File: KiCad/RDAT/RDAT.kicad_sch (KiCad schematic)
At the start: 17 parts

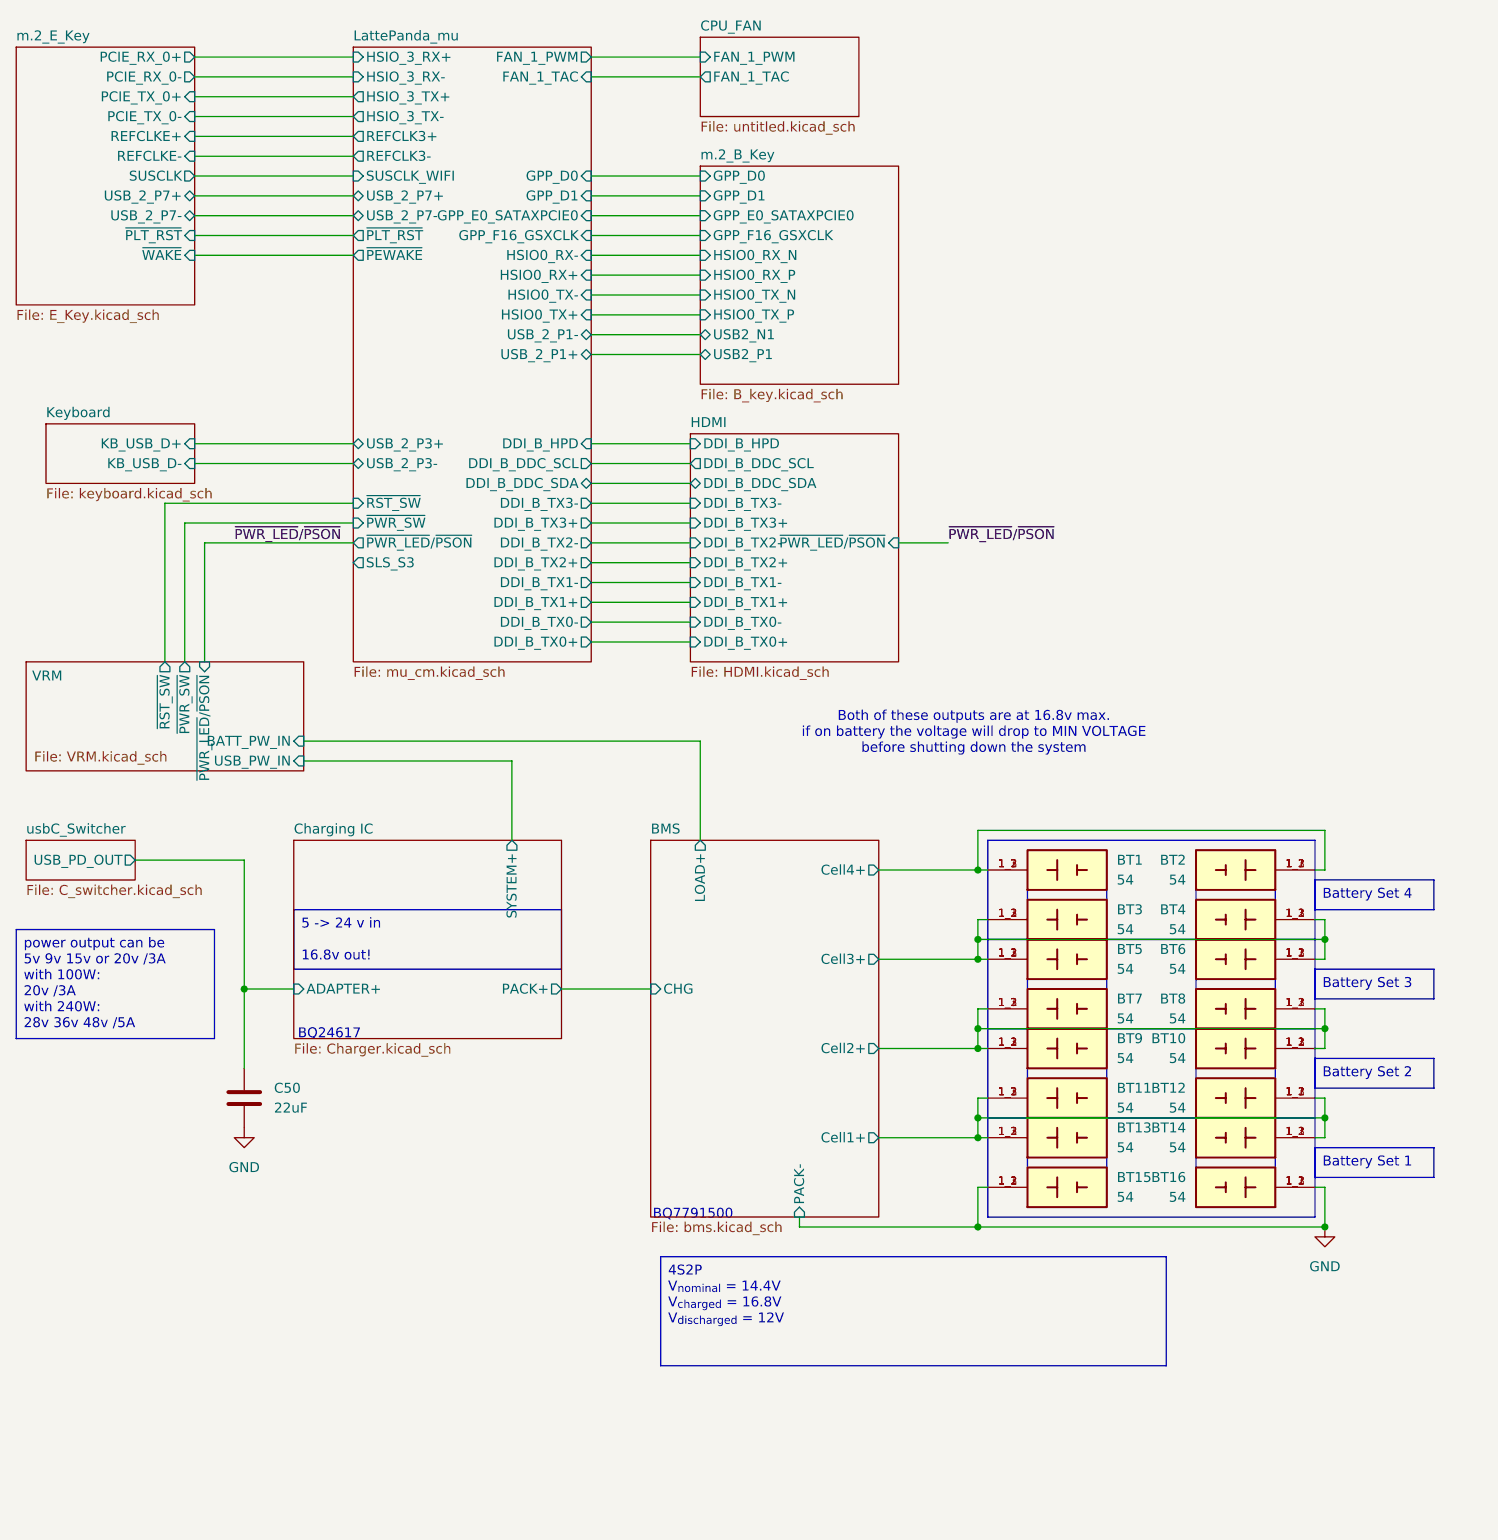
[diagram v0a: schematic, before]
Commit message: Started process of BMS review
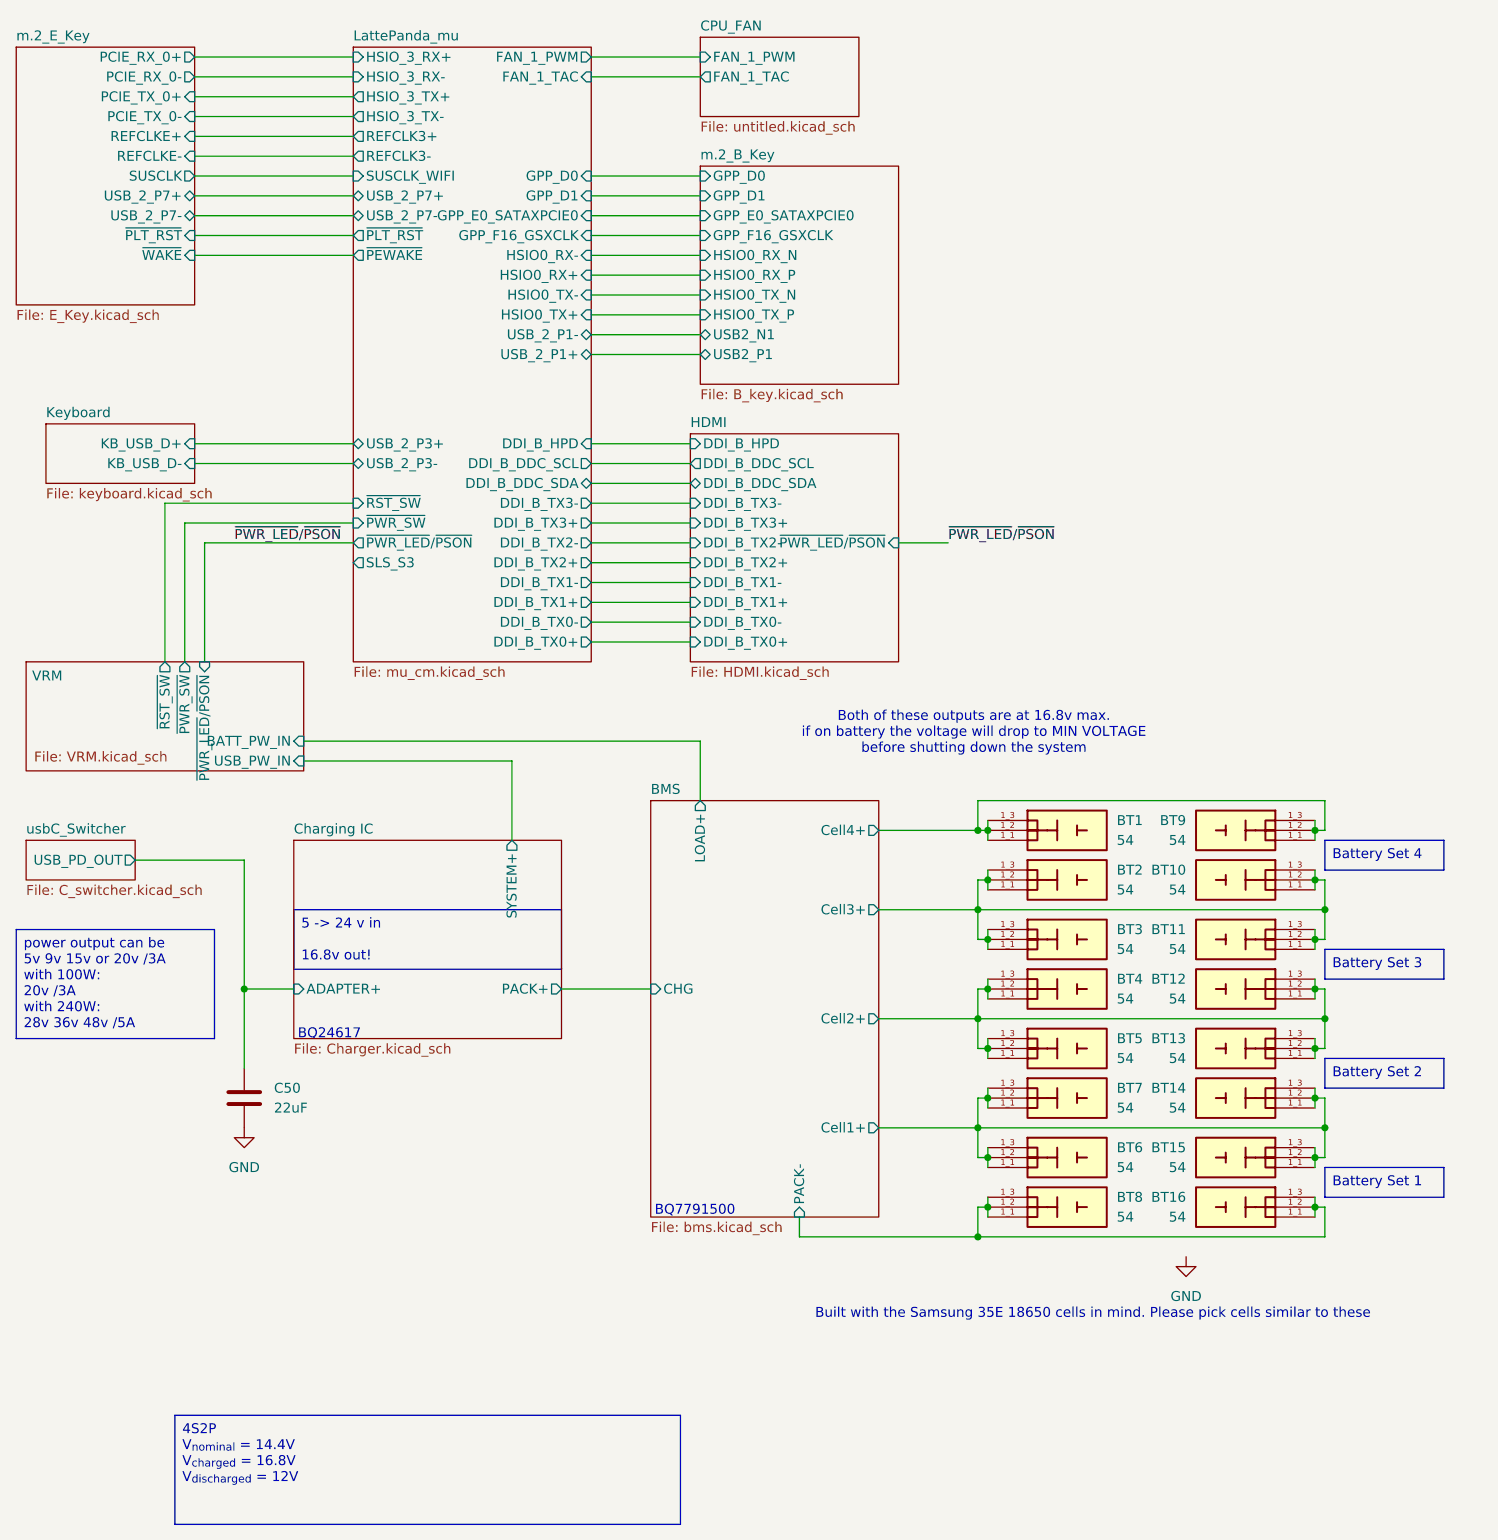
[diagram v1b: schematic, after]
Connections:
- net BMS/Cell1+: now also BT15.1_1, BT15.1_2, BT15.1_3, BT6.1_1, BT6.1_2, BT6.1_3, BT7.1_1, BT7.1_2, BT7.1_3; no longer BT11.1_1, BT11.1_2, BT11.1_3, BT12.1_1, BT12.1_2, BT12.1_3, BT13.1_1, BT13.1_2, BT13.1_3
- net BMS/Cell2+: now also BT12.1_1, BT12.1_2, BT12.1_3, BT13.1_1, BT13.1_2, BT13.1_3, BT4.1_1, BT4.1_2, BT4.1_3, BT5.1_1, BT5.1_2, BT5.1_3; no longer BT10.1_1, BT10.1_2, BT10.1_3, BT7.1_1, BT7.1_2, BT7.1_3, BT8.1_1, BT8.1_2, BT8.1_3, BT9.1_1, BT9.1_2, BT9.1_3
- net BMS/Cell3+: now also BT10.1_1, BT10.1_2, BT10.1_3, BT11.1_1, BT11.1_2, BT11.1_3, BT2.1_1, BT2.1_2, BT2.1_3; no longer BT4.1_1, BT4.1_2, BT4.1_3, BT5.1_1, BT5.1_2, BT5.1_3, BT6.1_1, BT6.1_2, BT6.1_3
- net BMS/Cell4+: now also BT9.1_1, BT9.1_2, BT9.1_3; no longer BT2.1_1, BT2.1_2, BT2.1_3
- net GND: no longer BT15.1_1, BT15.1_2, BT15.1_3, BT16.1_1, BT16.1_2, BT16.1_3
- new net BMS/PACK-: BT16.1_1, BT16.1_2, BT16.1_3, BT8.1_1, BT8.1_2, BT8.1_3
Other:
- note added: "Built with the Samsung 35E 18650 cells in mind. Please pick cells similar to these"

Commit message: 2x checked all schematics
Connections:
- net BMS/PACK- renamed Earth
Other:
- added sheet USBA_2.0 (usb.kicad_sch)
- sheet BMS ports: added SYS_BAT+, SYS_BAT-; removed CHG, LOAD+, PACK-
- sheet LattePanda_mu ports: added USB_2_P2+, USB_2_P2-, USB_2_P4+, USB_2_P4-; removed none

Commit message: Pre-Annotate FULL, add usb
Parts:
- BT1, BT10, BT11, BT12, BT13, BT14, BT15, BT16, BT2, BT3, BT4, BT5, BT6, BT7, BT8, BT9: JLCPCB_LINK (none) -> https://jlcpcb.com/partdetail/Keystone-54/C2685232
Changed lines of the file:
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@@
 			)
 		)
-		(property "Datasheet" ""
+		(property "Datasheet" "https://www.lcsc.com/datasheet/lcsc_datasheet_2103051836_Keystone-54_C2685232.pdf"
 			(at 173.99 116.84 0)
 			(effects
@@
 			)
 		)
+		(property "JLCPCB_LINK" "https://jlcpcb.com/partdetail/Keystone-54/C2685232"
+			(at 173.99 116.84 0)
+			(effects
+				(font
+					(size 1.27 1.27)
+				)
+				(hide yes)
+			)
+		)
 		(pin "1_3"
 		)
@@
 			)
 		)
-		(property "Datasheet" ""
+		(property "Datasheet" "https://www.lcsc.com/datasheet/lcsc_datasheet_2103051836_Keystone-54_C2685232.pdf"
 			(at 173.99 144.78 0)
 			(effects
@@
 			)
 		)
+		(property "JLCPCB_LINK" "https://jlcpcb.com/partdetail/Keystone-54/C2685232"
+			(at 173.99 144.78 0)
+			(effects
+				(font
+					(size 1.27 1.27)
+				)
+				(hide yes)
+			)
+		)
 		(pin "1_3"
 		)
@@
 			)
 		)
+		(property "JLCPCB_LINK" ""
+			(at 46.99 151.13 0)
+			(effects
+				(font
+					(size 1.27 1.27)
+				)
+			)
+		)
 		(pin "1"
 		)
@@
 			)
 		)
-		(property "Datasheet" ""
+		(property "Datasheet" "https://www.lcsc.com/datasheet/lcsc_datasheet_2103051836_Keystone-54_C2685232.pdf"
 			(at 173.99 151.13 0)
 			(effects
@@
 			)
 		)
+		(property "JLCPCB_LINK" "https://jlcpcb.com/partdetail/Keystone-54/C2685232"
+			(at 173.99 151.13 0)
+			(effects
+				(font
+					(size 1.27 1.27)
+				)
+				(hide yes)
+			)
+		)
 		(pin "1_3"
 		)
@@
 			)
 		)
-		(property "Datasheet" ""
+		(property "Datasheet" "https://www.lcsc.com/datasheet/lcsc_datasheet_2103051836_Keystone-54_C2685232.pdf"
 			(at 152.4 165.1 0)
 			(effects
@@
 			)
 		)
+		(property "JLCPCB_LINK" "https://jlcpcb.com/partdetail/Keystone-54/C2685232"
+			(at 152.4 165.1 0)
+			(effects
+				(font
+					(size 1.27 1.27)
+				)
+				(hide yes)
+			)
+		)
 		(pin "1_3"
 		)
@@
 			)
 		)
-		(property "Datasheet" ""
+		(property "Datasheet" "https://www.lcsc.com/datasheet/lcsc_datasheet_2103051836_Keystone-54_C2685232.pdf"
 			(at 173.99 130.81 0)
 			(effects
@@
 			)
 		)
+		(property "JLCPCB_LINK" "https://jlcpcb.com/partdetail/Keystone-54/C2685232"
+			(at 173.99 130.81 0)
+			(effects
+				(font
+					(size 1.27 1.27)
+				)
+				(hide yes)
+			)
+		)
 		(pin "1_3"
 		)
@@
 			)
 		)
-		(property "Datasheet" ""
+		(property "Datasheet" "https://www.lcsc.com/datasheet/lcsc_datasheet_2103051836_Keystone-54_C2685232.pdf"
 			(at 152.4 137.16 0)
 			(effects
@@
 			)
 		)
+		(property "JLCPCB_LINK" "https://jlcpcb.com/partdetail/Keystone-54/C2685232"
+			(at 152.4 137.16 0)
+			(effects
+				(font
+					(size 1.27 1.27)
+				)
+				(hide yes)
+			)
+		)
 		(pin "1_3"
 		)
@@
 			)
 		)
-		(property "Datasheet" ""
+		(property "Datasheet" "https://www.lcsc.com/datasheet/lcsc_datasheet_2103051836_Keystone-54_C2685232.pdf"
 			(at 152.4 116.84 0)
 			(effects
@@
 			)
 		)
+		(property "JLCPCB_LINK" "https://jlcpcb.com/partdetail/Keystone-54/C2685232"
+			(at 152.4 116.84 0)
+			(effects
+				(font
+					(size 1.27 1.27)
+				)
+				(hide yes)
+			)
+		)
 		(pin "1_3"
 		)
@@
 			)
 		)
-		(property "Datasheet" ""
+		(property "Datasheet" "https://www.lcsc.com/datasheet/lcsc_datasheet_2103051836_Keystone-54_C2685232.pdf"
 			(at 152.4 158.75 0)
 			(effects
@@
 			)
 		)
+		(property "JLCPCB_LINK" "https://jlcpcb.com/partdetail/Keystone-54/C2685232"
+			(at 152.4 158.75 0)
+			(effects
+				(font
+					(size 1.27 1.27)
+				)
+				(hide yes)
+			)
+		)
 		(pin "1_3"
 		)
@@
 			)
 		)
-		(property "Datasheet" ""
+		(property "Datasheet" "https://www.lcsc.com/datasheet/lcsc_datasheet_2103051836_Keystone-54_C2685232.pdf"
 			(at 173.99 158.75 0)
 			(effects
@@
 			)
 		)
+		(property "JLCPCB_LINK" "https://jlcpcb.com/partdetail/Keystone-54/C2685232"
+			(at 173.99 158.75 0)
+			(effects
+				(font
+					(size 1.27 1.27)
+				)
+				(hide yes)
+			)
+		)
 		(pin "1_3"
 		)
@@
 			)
 		)
-		(property "Datasheet" ""
+		(property "Datasheet" "https://www.lcsc.com/datasheet/lcsc_datasheet_2103051836_Keystone-54_C2685232.pdf"
 			(at 152.4 130.81 0)
 			(effects
@@
 			)
 		)
+		(property "JLCPCB_LINK" "https://jlcpcb.com/partdetail/Keystone-54/C2685232"
+			(at 152.4 130.81 0)
+			(effects
+				(font
+					(size 1.27 1.27)
+				)
+				(hide yes)
+			)
+		)
 		(pin "1_3"
 		)
@@
 			)
 		)
-		(property "Datasheet" ""
+		(property "Datasheet" "https://www.lcsc.com/datasheet/lcsc_datasheet_2103051836_Keystone-54_C2685232.pdf"
 			(at 173.99 137.16 0)
 			(effects
@@
 			)
 		)
+		(property "JLCPCB_LINK" "https://jlcpcb.com/partdetail/Keystone-54/C2685232"
+			(at 173.99 137.16 0)
+			(effects
+				(font
+					(size 1.27 1.27)
+				)
+				(hide yes)
+			)
+		)
 		(pin "1_3"
 		)
@@
 			)
 		)
-		(property "Datasheet" ""
+		(property "Datasheet" "https://www.lcsc.com/datasheet/lcsc_datasheet_2103051836_Keystone-54_C2685232.pdf"
 			(at 152.4 144.78 0)
 			(effects
@@
 			)
 		)
+		(property "JLCPCB_LINK" "https://jlcpcb.com/partdetail/Keystone-54/C2685232"
+			(at 152.4 144.78 0)
+			(effects
+				(font
+					(size 1.27 1.27)
+				)
+				(hide yes)
+			)
+		)
 		(pin "1_3"
 		)
@@
 			)
 		)
-		(property "Datasheet" ""
+		(property "Datasheet" "https://www.lcsc.com/datasheet/lcsc_datasheet_2103051836_Keystone-54_C2685232.pdf"
 			(at 152.4 151.13 0)
 			(effects
@@
 			)
 		)
+		(property "JLCPCB_LINK" "https://jlcpcb.com/partdetail/Keystone-54/C2685232"
+			(at 152.4 151.13 0)
+			(effects
+				(font
+					(size 1.27 1.27)
+				)
+				(hide yes)
+			)
+		)
 		(pin "1_3"
 		)
@@
 			)
 		)
-		(property "Datasheet" ""
+		(property "Datasheet" "https://www.lcsc.com/datasheet/lcsc_datasheet_2103051836_Keystone-54_C2685232.pdf"
 			(at 173.99 165.1 0)
 			(effects
@@
 			)
 		)
+		(property "JLCPCB_LINK" "https://jlcpcb.com/partdetail/Keystone-54/C2685232"
+			(at 173.99 165.1 0)
+			(effects
+				(font
+					(size 1.27 1.27)
+				)
+				(hide yes)
+			)
+		)
 		(pin "1_3"
 		)
@@
 			)
 		)
-		(property "Datasheet" ""
+		(property "Datasheet" "https://www.lcsc.com/datasheet/lcsc_datasheet_2103051836_Keystone-54_C2685232.pdf"
 			(at 173.99 123.19 0)
 			(effects
@@
 			)
 		)
+		(property "JLCPCB_LINK" "https://jlcpcb.com/partdetail/Keystone-54/C2685232"
+			(at 173.99 123.19 0)
+			(effects
+				(font
+					(size 1.27 1.27)
+				)
+				(hide yes)
+			)
+		)
 		(pin "1_3"
 		)
@@
 			)
 		)
-		(property "Datasheet" ""
+		(property "Datasheet" "https://www.lcsc.com/datasheet/lcsc_datasheet_2103051836_Keystone-54_C2685232.pdf"
 			(at 152.4 123.19 0)
 			(effects
@@
 				(hide yes)
 			)
+		)
+		(property "JLCPCB_LINK" "https://jlcpcb.com/partdetail/Keystone-54/C2685232"
+			(at 152.4 123.19 0)
+			(effects
+				(font
+					(size 1.27 1.27)
+				)
+				(hide yes)
+			)

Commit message: Added Libs and DOCS
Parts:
- BT1: footprint 54:BAT_54 -> footprints:BAT_BK-18650-CLIP
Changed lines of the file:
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@@
 			)
 		)
-		(property "Footprint" "54:BAT_54"
+		(property "Footprint" "footprints:BAT_BK-18650-CLIP"
 			(at 132.08 125.222 0)
 			(effects

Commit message: Sourced and documented all parts
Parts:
- BT10, BT11, BT12, BT13, BT14, BT15, BT16, BT2, BT3, BT4, BT5, BT6, BT7, BT8, BT9: footprint 54:BAT_54 -> footprints:BAT_BK-18650-CLIP
- C50: footprint (none) -> Capacitor_SMD:C_0805_2012Metric; JLCPCB_LINK (none) -> https://jlcpcb.com/partdetail/46786-CL21A226MAQNNNE/C45783
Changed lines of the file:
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@@
 			)
 		)
-		(property "Footprint" "54:BAT_54"
+		(property "Footprint" "footprints:BAT_BK-18650-CLIP"
 			(at 194.31 125.222 0)
 			(effects
@@
 			)
 		)
-		(property "Footprint" "54:BAT_54"
+		(property "Footprint" "footprints:BAT_BK-18650-CLIP"
 			(at 194.31 153.162 0)
 			(effects
@@
 			)
 		)
-		(property "Footprint" ""
+		(property "Footprint" "Capacitor_SMD:C_0805_2012Metric"
 			(at 47.9552 154.94 0)
 			(effects
@@
 			)
 		)
-		(property "Datasheet" "~"
+		(property "Datasheet" "https://jlcpcb.com/api/file/downloadByFileSystemAccessId/8579706866429190144"
 			(at 46.99 151.13 0)
 			(effects
@@
 			)
 		)
-		(property "JLCPCB_LINK" ""
+		(property "JLCPCB_LINK" "https://jlcpcb.com/partdetail/46786-CL21A226MAQNNNE/C45783"
 			(at 46.99 151.13 0)
 			(effects
@@
 					(size 1.27 1.27)
 				)
+				(hide yes)
 			)
 		)
@@
 			)
 		)
-		(property "Footprint" "54:BAT_54"
+		(property "Footprint" "footprints:BAT_BK-18650-CLIP"
 			(at 194.31 159.512 0)
 			(effects
@@
 			)
 		)
-		(property "Footprint" "54:BAT_54"
+		(property "Footprint" "footprints:BAT_BK-18650-CLIP"
 			(at 132.08 173.482 0)
 			(effects
@@
 			)
 		)
-		(property "Footprint" "54:BAT_54"
+		(property "Footprint" "footprints:BAT_BK-18650-CLIP"
 			(at 194.31 139.192 0)
 			(effects
@@
 			)
 		)
-		(property "Footprint" "54:BAT_54"
+		(property "Footprint" "footprints:BAT_BK-18650-CLIP"
 			(at 132.08 145.542 0)
 			(effects
@@
 			)
 		)
-		(property "Footprint" "54:BAT_54"
+		(property "Footprint" "footprints:BAT_BK-18650-CLIP"
 			(at 132.08 167.132 0)
 			(effects
@@
 			)
 		)
-		(property "Footprint" "54:BAT_54"
+		(property "Footprint" "footprints:BAT_BK-18650-CLIP"
 			(at 194.31 167.132 0)
 			(effects
@@
 			)
 		)
-		(property "Footprint" "54:BAT_54"
+		(property "Footprint" "footprints:BAT_BK-18650-CLIP"
 			(at 132.08 139.192 0)
 			(effects
@@
 			)
 		)
-		(property "Footprint" "54:BAT_54"
+		(property "Footprint" "footprints:BAT_BK-18650-CLIP"
 			(at 194.31 145.542 0)
 			(effects
@@
 			)
 		)
-		(property "Footprint" "54:BAT_54"
+		(property "Footprint" "footprints:BAT_BK-18650-CLIP"
 			(at 132.08 153.162 0)
 			(effects
@@
 			)
 		)
-		(property "Footprint" "54:BAT_54"
+		(property "Footprint" "footprints:BAT_BK-18650-CLIP"
 			(at 132.08 159.512 0)
 			(effects
@@
 			)
 		)
-		(property "Footprint" "54:BAT_54"
+		(property "Footprint" "footprints:BAT_BK-18650-CLIP"
 			(at 194.31 173.482 0)
 			(effects
@@
 			)
 		)
-		(property "Footprint" "54:BAT_54"
+		(property "Footprint" "footprints:BAT_BK-18650-CLIP"
 			(at 194.31 131.572 0)
 			(effects
@@
 			)
 		)
-		(property "Footprint" "54:BAT_54"
+		(property "Footprint" "footprints:BAT_BK-18650-CLIP"
 			(at 132.08 131.572 0)
 			(effects

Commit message: finalized board layout
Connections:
- no-connect marks 0 -> 1
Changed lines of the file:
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@@
 		(color 0 0 0 0)
 	)
+	(no_connect
+		(at 60.96 87.63)
+	)
 	(wire
 		(pts
@@
 	)
 	(label "~{PWR_LED}{slash}~{PSON}"
-		(at 46.0403 84.8146 0)
+		(at 45.72 85.09 0)
 		(effects
 			(font
